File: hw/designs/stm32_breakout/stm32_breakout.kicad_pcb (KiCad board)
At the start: 2 copper layers, 15.2 x 27.9 mm, 20 parts, among them J1 USB_B_Micro, J2 Conn_01x10_Male, J3 Conn_01x10_Male, J4 Conn_01x03_Male, U1 AP7361C-33E, U2 STM32L031F6Px, U3 KC2016Z, Y1 ABS25-32.768KHZ-6-T

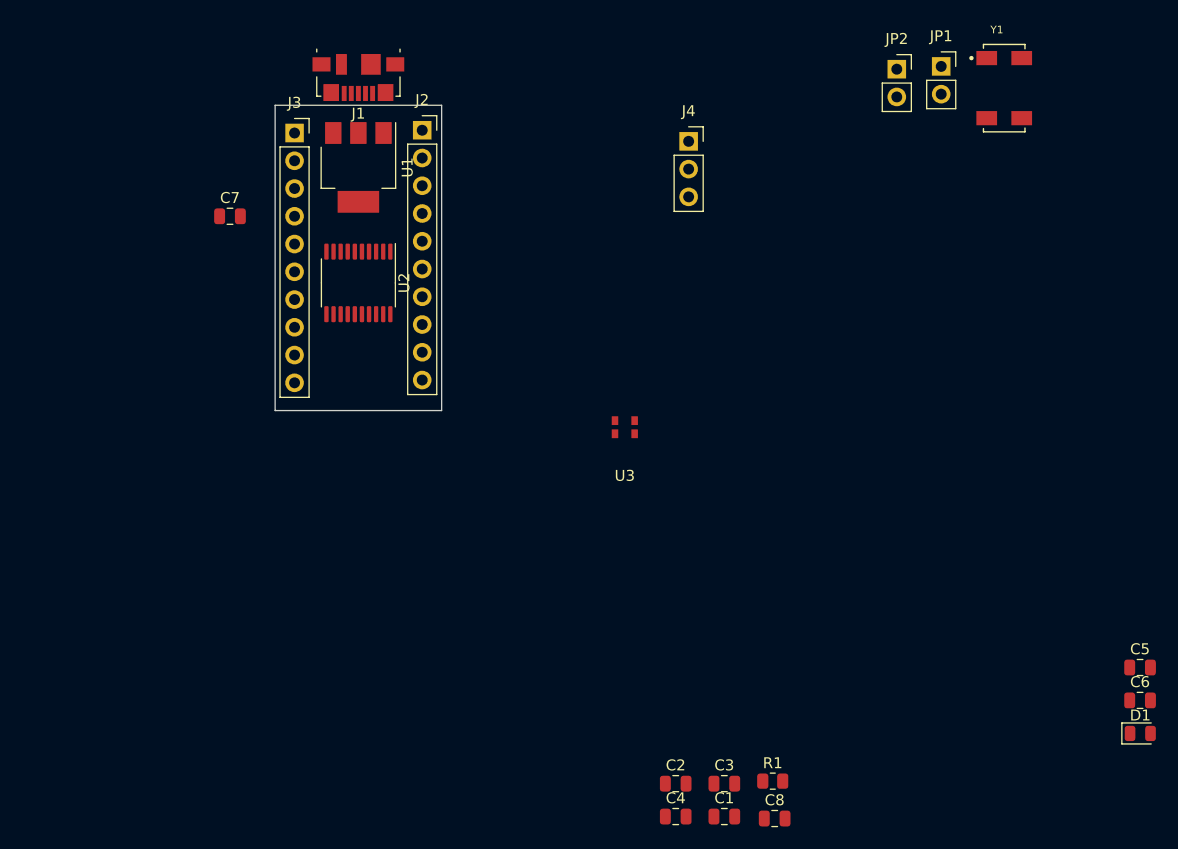
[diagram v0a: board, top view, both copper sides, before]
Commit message: Removed RTC circuit. Changed pinout on headers. Updated jumpers to resistors instead. Started routing
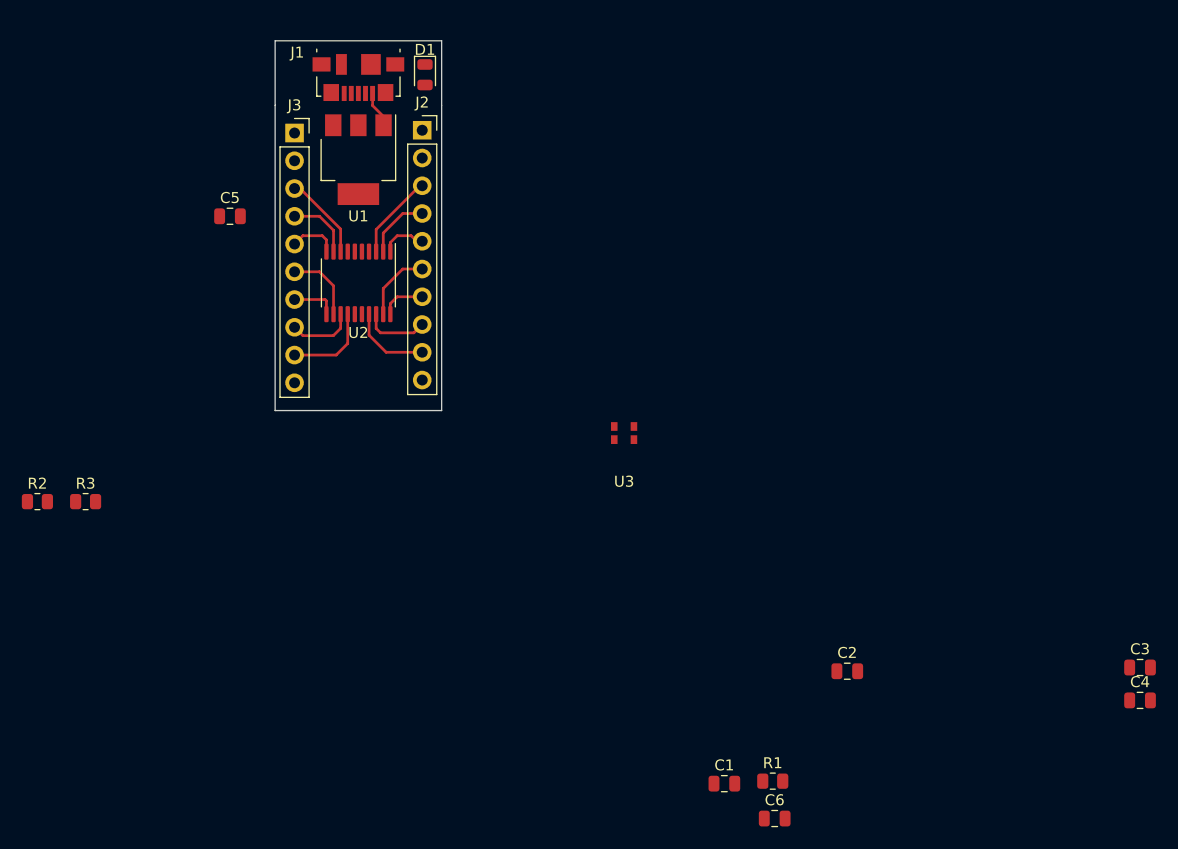
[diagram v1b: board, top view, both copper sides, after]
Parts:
- removed the C1 at (165.6, 128.6)
- removed the C2 at (161.1, 125.6)
- removed J4: Conn_01x03_Male, Connector_PinSocket_2.54mm:PinSocket_1x03_P2.54mm_Vertical
- removed JP1, JP2: Jumper, Connector_PinSocket_2.54mm:PinSocket_1x02_P2.54mm_Vertical
- removed Y1: ABS25-32.768KHZ-6-T, Custom:XTAL_ABS25-32.768KHZ-6-1-T
- added R2: 0, Resistor_SMD:R_0805_2012Metric, F.Cu at (102.7, 99.8)
- added R3: UNPOP, Resistor_SMD:R_0805_2012Metric, F.Cu at (107.1, 99.8)
- moved D1 89.0 mm to (138.2, 60.7), turned to 270 degrees
- moved C2 20.6 mm to (176.8, 115.3)
- moved U1 0.71 mm to (132.1, 68.5)
- moved U3 0.54 mm to (156.4, 93.5)
- renumbered C3 to C1, C4 to C2, C5 to C3, C6 to C4, C7 to C5, C8 to C6
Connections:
- J2 pad 1: +3V3 -> Net-(J2-Pad1)
- J2 pad 10: GND -> +3V3
- J2 pad 3: /PA13 -> /PC15-OSC32_OUT
- J2 pad 4: /PA14 -> /PC14-OSC32IN
- J2 pad 5: /PC14-OSC32IN -> /PB9-BOOT0
- J2 pad 6: /PC15-OSC32_OUT -> /PA13
- J2 pad 7: /PB1 -> /PA14
- J2 pad 8: /PB9-BOOT0 -> /PA10
- J2 pad 9: Net-(J2-Pad9) -> /PA9
- J3 pad 10: /PA10 -> GND
- J3 pad 6: /PA5 -> /PA6
- J3 pad 7: /PA6 -> /PA5
- J3 pad 9: /PA9 -> /PB1
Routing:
- net /PB1: track 0.00 -> 7.99 mm
- net /PC15-OSC32_OUT: track 0.00 -> 7.90 mm
- net /PA2: track 0.00 -> 7.82 mm
- net /PA9: track 0.00 -> 7.44 mm
- net /PA6: track 0.00 -> 6.70 mm
- net /PA13: track 0.00 -> 6.65 mm
- net /PA7: track 0.00 -> 6.11 mm
- net /PA3: track 0.00 -> 6.05 mm
- net /PC14-OSC32IN: track 0.00 -> 6.01 mm
- net /PA10: track 0.00 -> 6.00 mm
- net /PA4: track 0.00 -> 4.47 mm
- net /PB9-BOOT0: track 0.00 -> 4.21 mm
- net /PA5: track 0.00 -> 4.18 mm
- net /PA14: track 0.00 -> 4.14 mm
- net Net-(C1-Pad2): track 0.00 -> 4.03 mm
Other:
- board size 15.2 x 27.9 mm -> 15.2 x 33.8 mm

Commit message: Routing complete except for 3V3 and GND
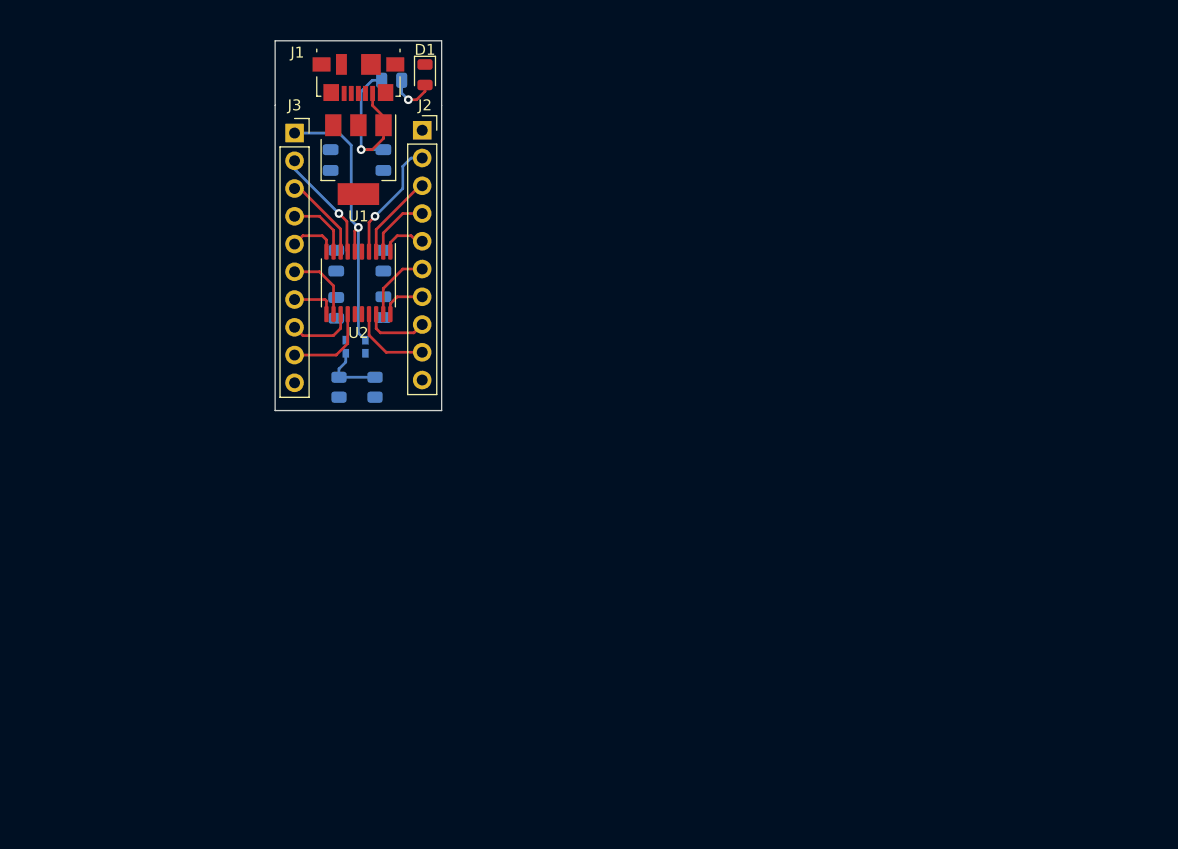
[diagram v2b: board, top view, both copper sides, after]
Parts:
- C1, C2, C3, C4, C5, C6, R1, R2, R3, U3: moved to B.Cu
- moved C3 82.5 mm to (130.0, 77.7), turned to 270 degrees
- moved C4 80.1 mm to (134.4, 77.7), turned to 270 degrees
- moved R1 73.0 mm to (135.1, 61.2), turned to 180 degrees
- moved C2 66.5 mm to (129.5, 68.5), turned to 90 degrees
- moved C1 65.0 mm to (134.4, 68.5), turned to 90 degrees
- moved C6 58.9 mm to (134.4, 82.0), turned to 90 degrees
- moved R2 32.6 mm to (133.6, 89.3), turned to 90 degrees
- moved U3 25.8 mm to (131.8, 85.6), turned to 180 degrees
- moved R3 25.4 mm to (130.3, 89.3), turned to 270 degrees
- moved C5 12.8 mm to (130.0, 82.0), turned to 90 degrees
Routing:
- net /PA0-CK_IN: track 0.00 -> 26.4 mm, vias 0 -> 1
- net Net-(C1-Pad2): track 4.03 -> 18.1 mm, vias 0 -> 1
- net /NRST: track 0.00 -> 11.2 mm, vias 0 -> 1
- net /PA1: track 0.00 -> 10.3 mm, vias 0 -> 1
- net Net-(R2-Pad2): track 0.00 -> 5.75 mm
- net Net-(D1-Pad2): track 0.00 -> 4.46 mm, vias 0 -> 1

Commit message: Board is complete. Needs review
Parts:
- moved C2 0.46 mm to (130.0, 68.5)
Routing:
- net GND: track 0.00 -> 120.7 mm, vias 0 -> 6
- net +3V3: track 0.00 -> 9.26 mm, vias 0 -> 2
- net /PA0-CK_IN: track 26.4 -> 24.0 mm
- net /PB9-BOOT0: track 4.21 -> 3.31 mm
- net /PC14-OSC32IN: track 6.01 -> 6.78 mm
- net /PA9: track 7.44 -> 8.09 mm
- net /PA7: track 6.11 -> 5.51 mm
- net /NRST: track 11.2 -> 10.6 mm
- added copper zone on B.Cu, net +3V3
- added copper zone on F.Cu, net GND

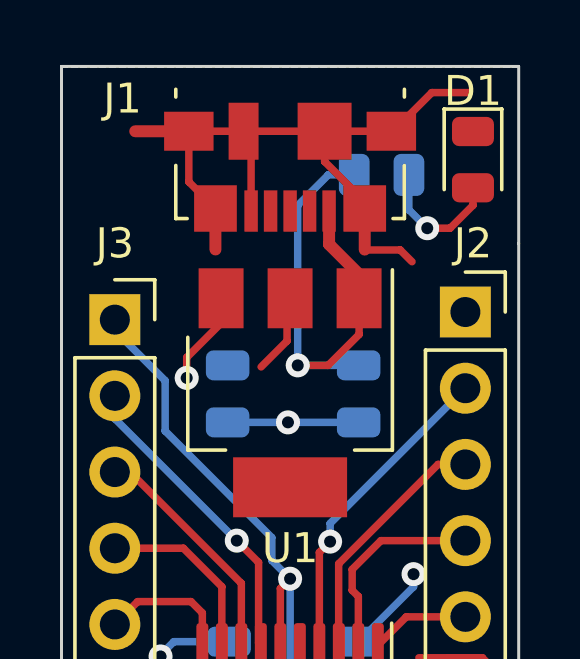
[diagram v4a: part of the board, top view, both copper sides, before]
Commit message: Updated PCB to address SOT223R part change
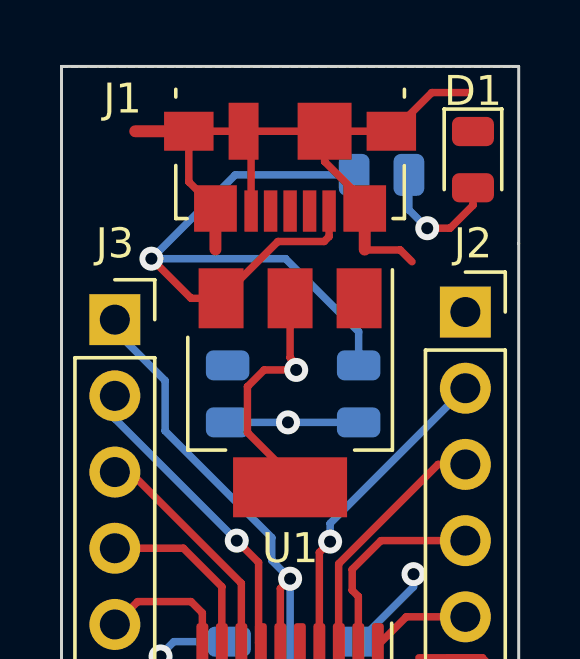
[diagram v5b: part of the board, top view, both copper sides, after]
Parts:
- U1: value AP7361C-33E -> AP7361C-33ER
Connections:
- U1 pad 1: Net-(C1-Pad2) -> GND
- U1 pad 2: GND -> +3V3
- U1 pad 3: +3V3 -> Net-(C1-Pad2)
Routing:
- net Net-(C1-Pad2): track 18.1 -> 26.0 mm
- net +3V3: track 9.26 -> 14.5 mm
- net GND: track 120.7 -> 119.8 mm
